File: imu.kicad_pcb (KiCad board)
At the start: 4 copper layers, 60.8 x 59.2 mm, 45 parts, among them J1 USB_C_Receptacle_USB2.0_16P, J2 JST_PH2.0_01x04, J3 JST_PH2.0_01x04, J4 GPIO0, J5 GPIO1, SW1 SW_Push, SW2 SW_Push, U1 LSM6DSL, U2 LIS2MDL, U3 AMS1117-3.3, U4 ESP32-C3-WROOM-02

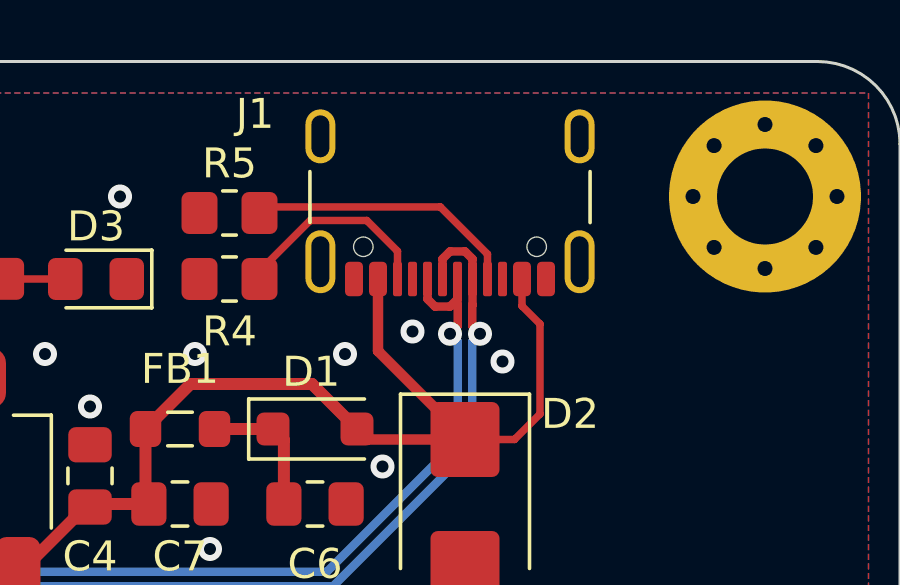
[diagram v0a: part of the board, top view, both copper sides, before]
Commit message: Connect USB-C Ground
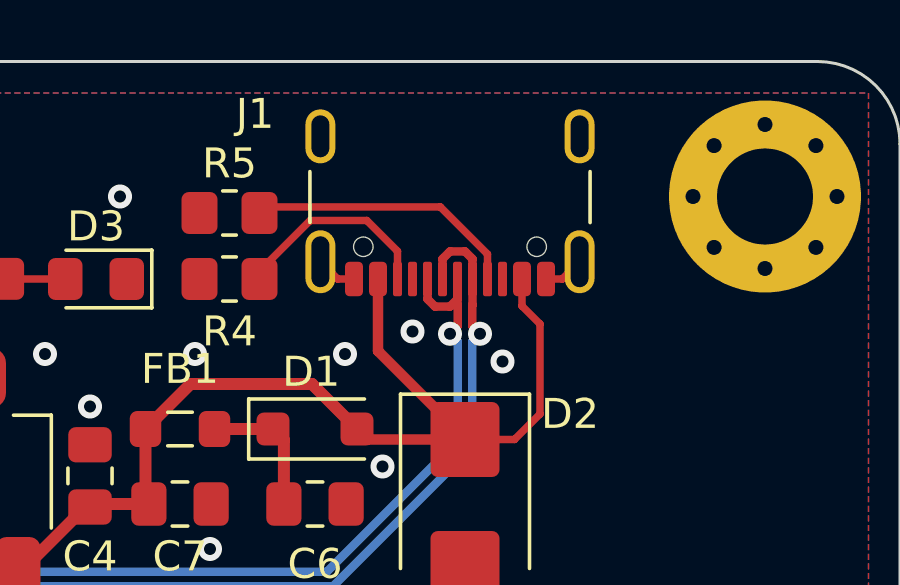
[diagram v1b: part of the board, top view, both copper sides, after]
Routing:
- net GND: track 47.7 -> 50.4 mm
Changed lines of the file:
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@@
+	)
+	(segment
+		(start 157.255 46)
+		(end 156.68 45.425)
+		(width 0.25)
+		(layer "F.Cu")
+		(net 1)
 	)
 	(segment
 		(start 146.45 88.25)
 		(end 146.6 88.4)
+		(width 0.25)
+		(layer "F.Cu")
+		(net 1)
+	)
+	(segment
+		(start 157.8 46)
+		(end 157.255 46)
 		(width 0.25)
 		(layer "F.Cu")
@@
 		(start 149.5885 67.9125)
 		(end 146.6625 67.9125)
+		(width 0.25)
+		(layer "F.Cu")
+		(net 1)
+	)
+	(segment
+		(start 164.2 46)
+		(end 164.745 46)
 		(width 0.25)
 		(layer "F.Cu")
@@
 		(width 0.25)
 		(layer "F.Cu")
+		(net 1)
+	)
+	(segment
+		(start 164.745 46)
+		(end 165.32 45.425)
+		(width 0.25)
+		(layer "F.Cu")

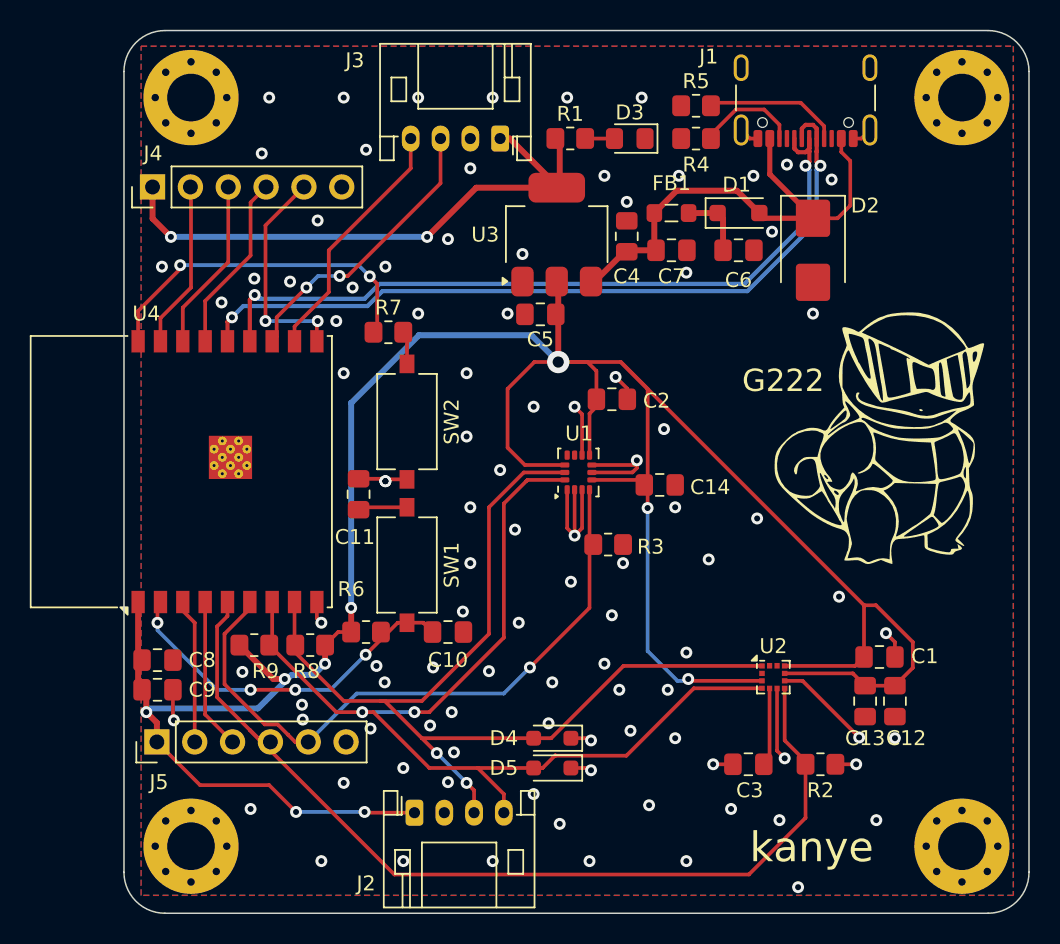
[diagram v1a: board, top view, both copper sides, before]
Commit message: Add Silkscreen Labels for Pin Headers
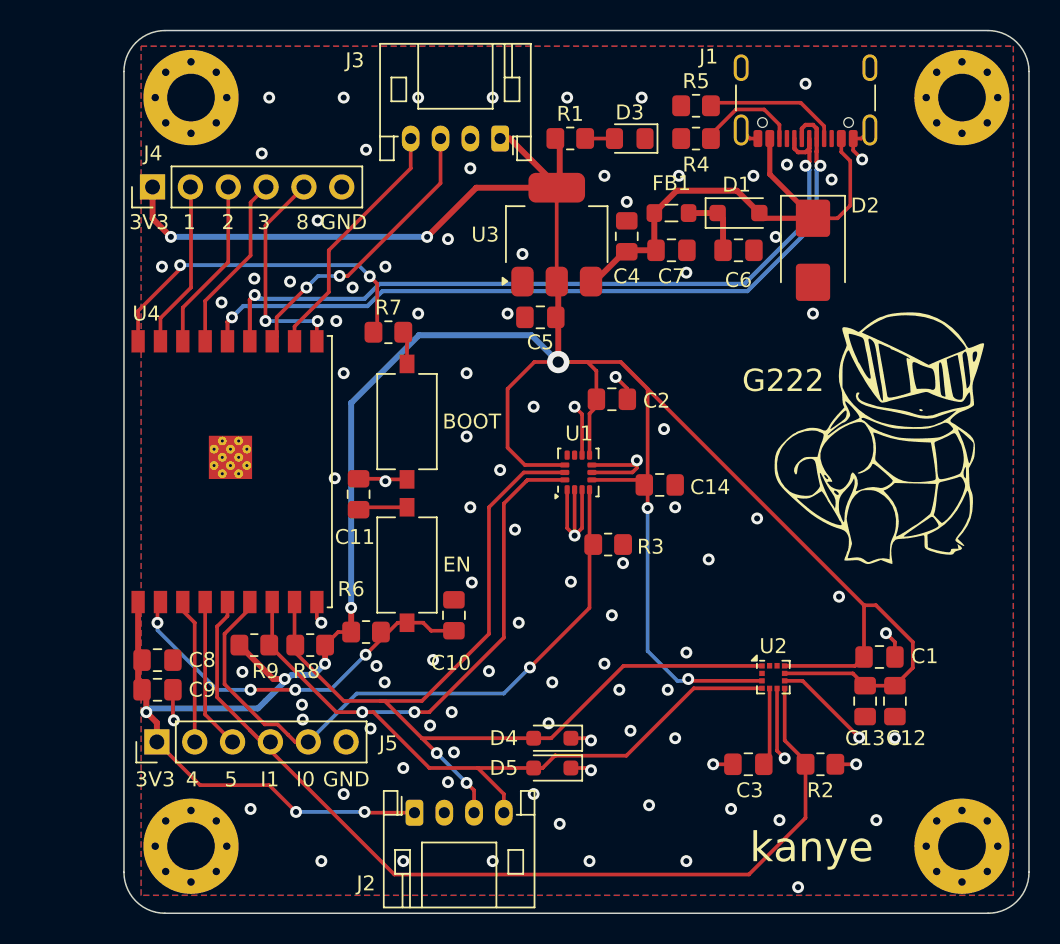
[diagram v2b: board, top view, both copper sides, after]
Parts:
- moved C10 1.19 mm to (137.4, 78.0), turned to 90 degrees
- moved C5 0.20 mm to (143.2, 58.0)
- renumbered SW2 to BOOT, SW1 to EN
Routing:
- net +3V3: track 233.1 -> 239.4 mm
- net GND: track 50.4 -> 52.0 mm, vias 99 -> 100
- net EN: track 24.2 -> 25.6 mm
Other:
- board text added: "1"
- board text added: "2"
- board text added: "3"
- board text added: "3V3"
- board text added: "4"
- board text added: "5"
- board text added: "8"
- board text added: "GND"
- board text added: "I0"
- board text added: "I1"

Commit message: Finall Fullboard V1
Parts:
- D2: value D_TVS -> D_TVS0
- D4, D5: value D_TVS -> D_TVS1
- renumbered EN to SW1, BOOT to SW2
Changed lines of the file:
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@@
 		(descr "Tactile switch, SPST, 6.0x3.5 mm, H2.5 mm, straight, NO, gull wing leads: https://www.ckswitches.com/media/2779/pts636.pdf")
 		(tags "switch tactile SPST 1P1T straight NO SMTR C&K")
-		(property "Reference" "EN"
-			(at -0.025 -3.35 0)
+		(property "Reference" "SW1"
+			(at -0.025 -4.15 0)
 			(unlocked yes)
 			(layer "F.SilkS")
@@
 		(descr "Tactile switch, SPST, 6.0x3.5 mm, H2.5 mm, straight, NO, gull wing leads: https://www.ckswitches.com/media/2779/pts636.pdf")
 		(tags "switch tactile SPST 1P1T straight NO SMTR C&K")
-		(property "Reference" "BOOT"
+		(property "Reference" "SW2"
 			(at 0 4.35 0)
 			(unlocked yes)
@@
 			)
 		)
-		(property "Value" "D_TVS"
+		(property "Value" "D_TVS1"
 			(at 0.1 1.9 0)
 			(layer "F.Fab")
@@
 			)
 		)
-		(property "Value" "D_TVS"
+		(property "Value" "D_TVS0"
 			(at 0 3.1 90)
 			(layer "F.Fab")
@@
 			)
 		)
-		(property "Value" "D_TVS"
+		(property "Value" "D_TVS1"
 			(at 0.1 1.9 0)
 			(layer "F.Fab")
